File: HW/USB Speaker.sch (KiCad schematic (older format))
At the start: 1 part, among them U1 PCM2707C

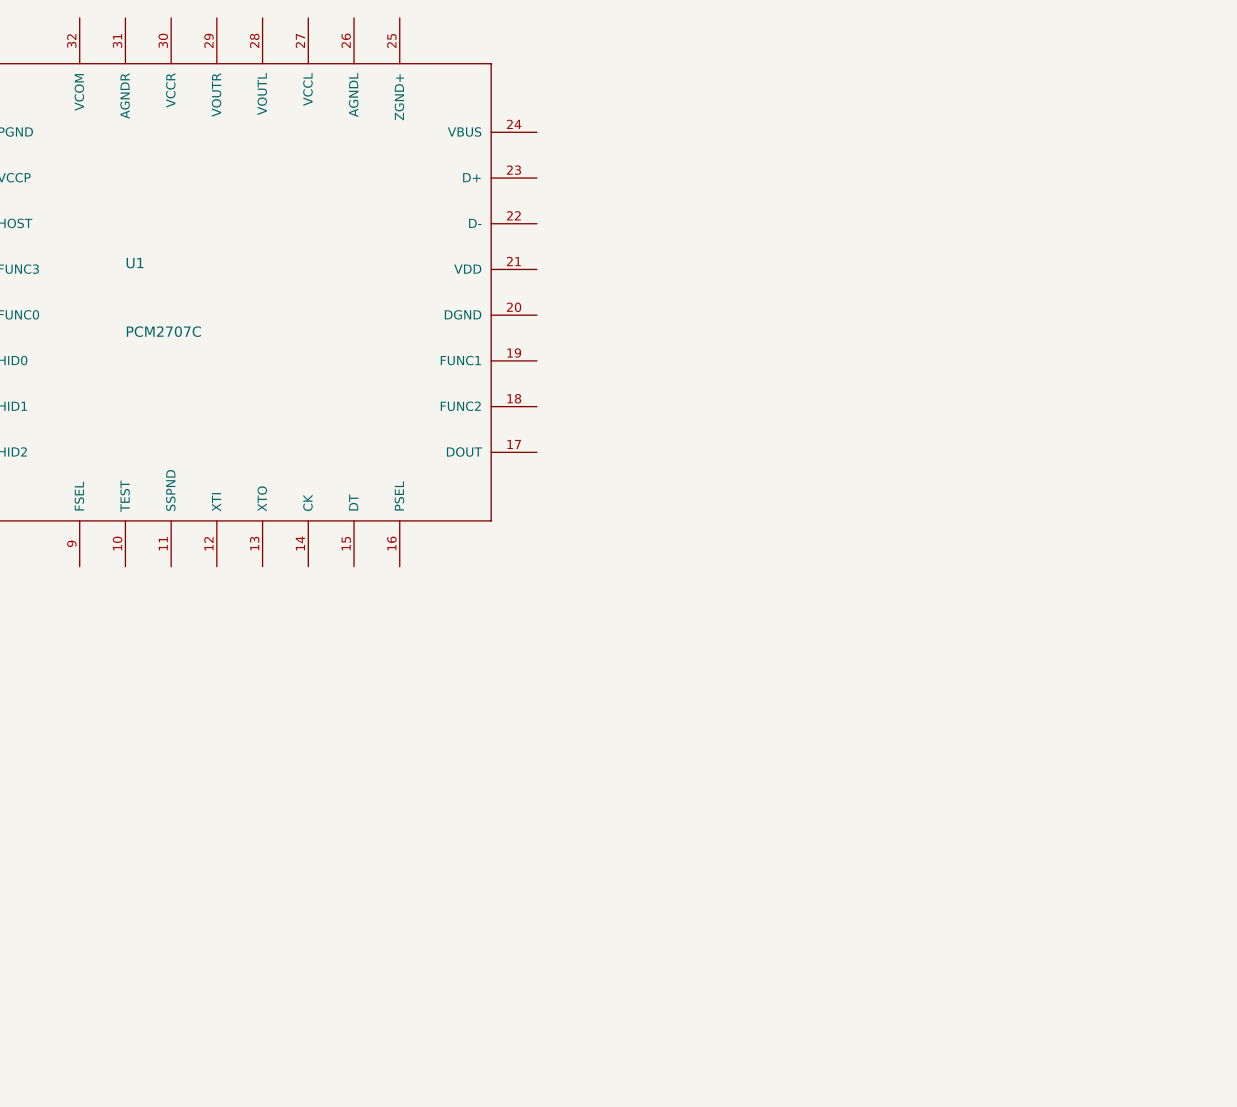
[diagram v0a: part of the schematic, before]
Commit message: Clock and USB circuits
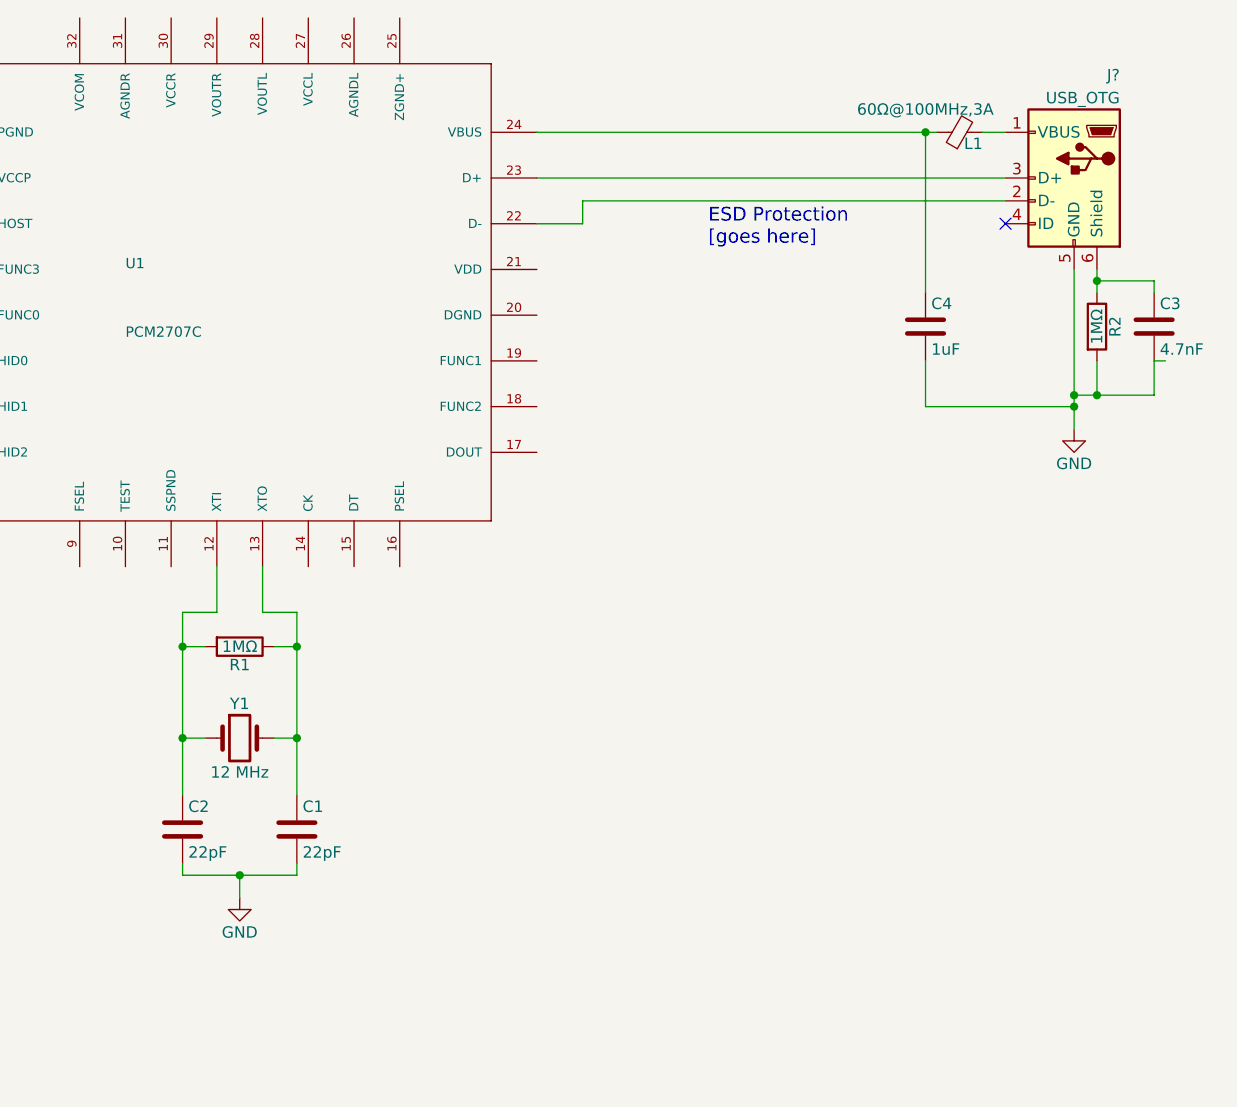
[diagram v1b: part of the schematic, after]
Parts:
- added C1, C2: 22pF, symbol C
- added C3: 4.7nF, symbol C
- added C4: 1uF, symbol C
- added J?: USB_OTG, symbol USB_OTG
- added L1: 60Ω@100MHz,3A, symbol Ferrite_Bead_Small
- added R1, R2: 1MΩ, symbol R
- added Y1: 12 MHz, symbol Crystal
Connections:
- net at U1.12 (XTI): now also C2.1, R1.2, Y1.1
- net at U1.13 (XTO): now also C1.1, R1.1, Y1.2
- net at U1.22 (D-): now also J?.2 (D-)
- net at U1.23 (D+): now also J?.3 (D+)
- net at U1.24 (VBUS): now also C4.1, L1.1
- new net: J?.1 (VBUS), L1.2
- new net: C3.1, J?.6 (Shield), R2.1
- new net GND: C1.2, C2.2, C3.2, C4.2, J?.5 (GND), R2.2
- no-connect marks 0 -> 1
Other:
- note added: "ESD Protection\n[goes here]\n"
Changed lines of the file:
@@
 LIBS:valves
 LIBS:PCM2707
+LIBS:USB Speaker-cache
 EELAYER 25 0
 EELAYER END
@@
 	1    0    0    -1
 $EndComp
+$Comp
+L Crystal Y1
+U 1 1 5B18799E
+P 5600 5250
+F 0 "Y1" H 5600 5400 50  0000 C CNN
+F 1 "12 MHz" H 5600 5100 50  0000 C CNN
+F 2 "" H 5600 5250 50  0001 C CNN
+F 3 "" H 5600 5250 50  0001 C CNN
+	1    5600 5250
+	1    0    0    -1
+$EndComp
+Wire Wire Line
+	5700 4500 5700 4700
+Wire Wire Line
+	5700 4700 5850 4700
+Wire Wire Line
+	5500 4700 5500 4500
+Wire Wire Line
+	5350 4700 5500 4700
+Wire Wire Line
+	5350 4700 5350 5500
+$Comp
+L R R1
+U 1 1 5B187A93
+P 5600 4850
+F 0 "R1" V 5680 4850 50  0000 C CNN
+F 1 "1MΩ" V 5600 4850 50  0000 C CNN
+F 2 "" V 5530 4850 50  0001 C CNN
+F 3 "" H 5600 4850 50  0001 C CNN
+	1    5600 4850
+	0    1    1    0
+$EndComp
+Wire Wire Line
+	5850 5250 5750 5250
+Wire Wire Line
+	5350 5250 5450 5250
+Wire Wire Line
+	5450 4850 5350 4850
+Connection ~ 5350 4850
+Wire Wire Line
+	5750 4850 5850 4850
+Connection ~ 5850 4850
+$Comp
+L C C2
+U 1 1 5B187E21
+P 5350 5650
+F 0 "C2" H 5375 5750 50  0000 L CNN
+F 1 "22pF" H 5375 5550 50  0000 L CNN
+F 2 "" H 5388 5500 50  0001 C CNN
+F 3 "" H 5350 5650 50  0001 C CNN
+	1    5350 5650
+	1    0    0    -1
+$EndComp
+$Comp
+L C C1
+U 1 1 5B187E62
+P 5850 5650
+F 0 "C1" H 5875 5750 50  0000 L CNN
+F 1 "22pF" H 5875 5550 50  0000 L CNN
+F 2 "" H 5888 5500 50  0001 C CNN
+F 3 "" H 5850 5650 50  0001 C CNN
+	1    5850 5650
+	1    0    0    -1
+$EndComp
+Connection ~ 5850 5250
+Connection ~ 5350 5250
+$Comp
+L GND #PWR?
+U 1 1 5B187EF0
+P 5600 5950
+F 0 "#PWR?" H 5600 5700 50  0001 C CNN
+F 1 "GND" H 5600 5800 50  0000 C CNN
+F 2 "" H 5600 5950 50  0001 C CNN
+F 3 "" H 5600 5950 50  0001 C CNN
+	1    5600 5950
+	1    0    0    -1
+$EndComp
+Wire Wire Line
+	5600 5950 5600 5850
+Wire Wire Line
+	5350 5850 5850 5850
+Wire Wire Line
+	5350 5850 5350 5800
+Wire Wire Line
+	5850 5850 5850 5800
+Connection ~ 5600 5850
+Wire Wire Line
+	5850 4700 5850 5500
+$Comp
+L USB_OTG J?
+U 1 1 5B18860C
+P 9250 2800
+F 0 "J?" H 9050 3250 50  0000 L CNN
+F 1 "USB_OTG" H 9050 3150 50  0000 L CNN
+F 2 "" H 9400 2750 50  0001 C CNN
+F 3 "" H 9400 2750 50  0001 C CNN
+	1    9250 2800
+	-1   0    0    -1
+$EndComp
+$Comp
+L GND #PWR?
+U 1 1 5B188764
+P 9250 3900
+F 0 "#PWR?" H 9250 3650 50  0001 C CNN
+F 1 "GND" H 9250 3750 50  0000 C CNN
+F 2 "" H 9250 3900 50  0001 C CNN
+F 3 "" H 9250 3900 50  0001 C CNN
+	1    9250 3900
+	1    0    0    -1
+$EndComp
+$Comp
+L R R2
+U 1 1 5B1887B9
+P 9350 3450
+F 0 "R2" V 9430 3450 50  0000 C CNN
+F 1 "1MΩ" V 9350 3450 50  0000 C CNN
+F 2 "" V 9280 3450 50  0001 C CNN
+F 3 "" H 9350 3450 50  0001 C CNN
+	1    9350 3450
+	1    0    0    -1
+$EndComp
+Wire Wire Line
+	9250 3200 9250 3900
+Wire Wire Line
+	9250 3750 9600 3750
+Wire Wire Line
+	9350 3200 9350 3300
+Wire Wire Line
+	9350 3750 9350 3600
+Connection ~ 9250 3800
+$Comp
+L C C3
+U 1 1 5B188B22
+P 9600 3450
+F 0 "C3" H 9625 3550 50  0000 L CNN
+F 1 "4.7nF" H 9625 3350 50  0000 L CNN
+F 2 "" H 9638 3300 50  0001 C CNN
+F 3 "" H 9600 3450 50  0001 C CNN
+	1    9600 3450
+	1    0    0    -1
+$EndComp
+Wire Wire Line
+	9600 3250 9600 3300
+Wire Wire Line
+	9600 3250 9350 3250
+Connection ~ 9350 3250
+Wire Wire Line
+	9600 3600 9650 3600
+Wire Wire Line
+	9600 3750 9600 3600
+Connection ~ 9350 3750
+NoConn ~ 8950 3000
+$Comp
+L C C4
+U 1 1 5B189480
+P 8600 3450
+F 0 "C4" H 8625 3550 50  0000 L CNN
+F 1 "1uF" H 8625 3350 50  0000 L CNN
+F 2 "" H 8638 3300 50  0001 C CNN
+F 3 "" H 8600 3450 50  0001 C CNN
+	1    8600 3450
+	1    0    0    -1
+$EndComp
+Wire Wire Line
+	8600 3600 8600 3800
+$Comp
+L Ferrite_Bead_Small L1
+U 1 1 5B1895A4
+P 8750 2600
+F 0 "L1" V 8700 2500 50  0000 L CNN
+F 1 "60Ω@100MHz,3A" V 8850 3050 50  0000 R CNN
+F 2 "" V 8680 2600 50  0001 C CNN
+F 3 "" H 8750 2600 50  0001 C CNN
+	1    8750 2600
+	0    -1   -1   0
+$EndComp
+Wire Wire Line
+	8950 2600 8850 2600
+Wire Wire Line
+	6900 2800 8950 2800
+Wire Wire Line
+	8950 2900 7100 2900
+Wire Wire Line
+	7100 2900 7100 3000
+Wire Wire Line
+	7100 3000 6900 3000
+Text Notes 7650 3100 0    60   ~ 0
+ESD Protection\n[goes here]\n
+Wire Wire Line
+	6900 2600 8650 2600
+Wire Wire Line
+	8600 3300 8600 2600
+Connection ~ 8600 2600
+Connection ~ 9250 3750
+Wire Wire Line
+	8600 3800 9250 3800
 $EndSCHEMATC

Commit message: DAC circuit
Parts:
- added C10, C11: 0.022uF, symbol C
- added C12, C13: 100uF, symbol CP1
- added C5, C6, C7, C9: 1uF, symbol C
- added C8: 10uF, symbol CP1
- added L2, L3: 60Ω@100MHz,3A, symbol Ferrite_Bead_Small
- added R10, R11, R12, R9: 3.3K, symbol R
- added R3, R6: 1.5K, symbol R
- added R4, R5: 22, symbol R
- added R7, R8: 16, symbol R
- R2: value 1MΩ -> 1M
- gave numbers to parts that had none: 1
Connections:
- net GND: now also U1.20 (DGND), U1.25 (ZGND+), C9.2, L2.2, L3.2, R10.2, R11.2, R12.2, R7.2, R8.2, R9.2
- net AGND_DAC: now reaches U1.1 (PGND)
- net AGND_DAC: now also C7.2, C8.2, L3.1
- net VDD: now reaches U1.10 (TEST)
- net VDD: now also U1.16 (PSEL), U1.21 (VDD), U1.3 (HOST), C9.1, R3.1, R6.1
- net at U1.15 (DT): now also R3.2
- net at U1.2 (VCCP): now also C7.1
- net at U1.22 (D-): now also R5.2; no longer J1.2 (D-)
- net at U1.23 (D+): now also R4.2; no longer J1.3 (D+)
- net AGND_LR: now reaches U1.26 (AGNDL)
- net AGND_LR: now also U1.31 (AGNDR), C5.1, C6.1, L2.1
- net at U1.27 (VCCL): now also C5.2
- net at U1.28 (VOUTL): now also C11.1, C13.1, R10.1
- net at U1.29 (VOUTR): now also C10.1, C12.1, R9.1
- net at U1.30 (VCCR): now also C6.2
- net at U1.32 (VCOM): now also C8.1
- new net: C10.2, R7.1
- new net: C11.2, R8.1
- new net: C12.2, R11.1
- new net: C13.2, R12.1
- new net USB_Dn: J1.2 (D-), R5.1
- new net USB_Dp: J1.3 (D+), R4.1, R6.2
- no-connect marks 1 -> 2
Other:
- moved on the sheet: C1, C2, C3, C4, J1, L1, R1, R2, U1, Y1

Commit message: DAC circuit edits and op-amp symbol creation
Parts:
- added R13: NP, symbol R
- added R14: 0.0, symbol R
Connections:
- net GND: now also R14.2
- net VDD: now also R13.1; no longer U1.3 (HOST)
- net SSPNDn: now reaches U1.11 (SSPND)
- net DOUT: now reaches U1.17 (DOUT)
- net FUNC2: now reaches U1.18 (FUNC2)
- net FUNC1: now reaches U1.19 (FUNC1)
- net FUNC3: now reaches U1.4 (FUNC3)
- net FUNC0: now reaches U1.5 (FUNC0)
- net HID0: now reaches U1.6 (HID0)
- net HID1: now reaches U1.7 (HID1)
- net HID2: now reaches U1.8 (HID2)
- net FSEL: now reaches U1.9 (FSEL)
- net Vout_L: now reaches C12.2, R11.1
- net Vout_R: now reaches C13.2, R12.1
- new net: R13.2, R14.1, U1.3 (HOST)
- no-connect marks 2 -> 11
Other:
- moved on the sheet: C7, L3

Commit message: Amplifier circuit using TPA6211A1-Q1
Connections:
- net VBUS: now reaches C4.1, L1.1, U1.24 (VBUS)
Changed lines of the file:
@@
 L VDD #PWR?
 U 1 1 5B1A7528
-P 5900 2400
-F 0 "#PWR?" H 5900 2250 50  0001 C CNN
-F 1 "VDD" H 5900 2550 50  0000 C CNN
-F 2 "" H 5900 2400 50  0001 C CNN
-F 3 "" H 5900 2400 50  0001 C CNN
-	1    5900 2400
+P 5900 2500
+F 0 "#PWR?" H 5900 2350 50  0001 C CNN
+F 1 "VDD" H 5900 2650 50  0000 C CNN
+F 2 "" H 5900 2500 50  0001 C CNN
+F 3 "" H 5900 2500 50  0001 C CNN
+	1    5900 2500
 	1    0    0    -1
 $EndComp
@@
 	3850 5100 4000 5100
 Wire Wire Line
-	3850 5100 3850 5900
+	3850 5100 3850 5250
+Wire Wire Line
+	3850 5250 3850 5650
+Wire Wire Line
+	3850 5650 3850 5900
 Wire Wire Line
 	4350 5650 4250 5650
@@
 	4100 6350 4100 6250
 Wire Wire Line
-	3850 6250 4350 6250
+	3850 6250 4100 6250
+Wire Wire Line
+	4100 6250 4350 6250
 Wire Wire Line
 	3850 6250 3850 6200
@@
 Connection ~ 4100 6250
 Wire Wire Line
-	4350 5100 4350 5900
-Wire Wire Line
-	7750 3600 7750 4300
-Wire Wire Line
-	7750 4150 8100 4150
-Wire Wire Line
-	7850 3600 7850 3700
+	4350 5100 4350 5250
+Wire Wire Line
+	4350 5250 4350 5650
+Wire Wire Line
+	4350 5650 4350 5900
+Wire Wire Line
+	7750 3600 7750 4150
+Wire Wire Line
+	7750 4150 7750 4200
+Wire Wire Line
+	7750 4200 7750 4300
+Wire Wire Line
+	7750 4150 7850 4150
+Wire Wire Line
+	7850 4150 8100 4150
+Wire Wire Line
+	7850 3600 7850 3650
+Wire Wire Line
+	7850 3650 7850 3700
 Wire Wire Line
 	7850 4150 7850 4000
@@
 	7450 3000 7350 3000
 Wire Wire Line
-	5400 3000 7150 3000
+	5400 3000 5650 3000
+Wire Wire Line
+	5650 3000 7100 3000
+Wire Wire Line
+	7100 3000 7150 3000
 Wire Wire Line
 	7100 3700 7100 3000
@@
 	7100 4200 7750 4200
 Wire Wire Line
-	3600 1800 5050 1800
+	3600 1800 3800 1800
+Wire Wire Line
+	3800 1800 4400 1800
+Wire Wire Line
+	4400 1800 4600 1800
+Wire Wire Line
+	4600 1800 5050 1800
 Wire Wire Line
 	3600 1800 3600 2500
@@
 Connection ~ 3800 1800
 Wire Wire Line
-	1650 2750 1650 3350
+	1650 2750 1650 3000
+Wire Wire Line
+	1650 3000 1650 3200
+Wire Wire Line
+	1650 3200 1650 3350
 Wire Wire Line
 	1900 3200 1650 3200
@@
 	4800 5100 5400 5100
 Wire Wire Line
-	5400 4900 5400 5200
+	5400 4900 5400 5100
+Wire Wire Line
+	5400 5100 5400 5200
 Wire Wire Line
 	2200 3200 2800 3200
@@
 	6450 3650 6450 3600
 Wire Wire Line
-	6050 3650 6450 3650
+	6050 3650 6300 3650
+Wire Wire Line
+	6300 3650 6450 3650
 Wire Wire Line
 	6300 3650 6300 3700
@@
 	6050 3800 6050 4050
 Wire Wire Line
-	6300 4000 6300 4100
+	6300 4000 6300 4050
+Wire Wire Line
+	6300 4050 6300 4100
 Wire Wire Line
 	6050 4050 6300 4050
@@
 	5400 3400 5500 3400
 Wire Wire Line
-	5800 3200 7450 3200
+	5800 3200 5900 3200
+Wire Wire Line
+	5900 3200 7450 3200
 Wire Wire Line
 	5800 3400 5900 3400
@@
 	2750 3000 2750 3000
 Wire Wire Line
-	5900 2400 5900 2550
+	5900 2500 5900 2550
 Wire Wire Line
 	5900 2850 5900 3200
@@
 	4000 850  4000 2500
 Wire Wire Line
-	4000 850  7550 850
+	4000 850  6200 850
+Wire Wire Line
+	6200 850  7150 850
+Wire Wire Line
+	7150 850  7550 850
 Wire Wire Line
 	4200 1100 4200 2500
 Wire Wire Line
-	4200 1100 7550 1100
-Wire Wire Line
-	7850 850  8900 850
-Wire Wire Line
-	7850 1100 8900 1100
+	4200 1100 6650 1100
+Wire Wire Line
+	6650 1100 7350 1100
+Wire Wire Line
+	7350 1100 7550 1100
+Wire Wire Line
+	7850 850  8200 850
+Wire Wire Line
+	8200 850  8900 850
+Wire Wire Line
+	7850 1100 8400 1100
+Wire Wire Line
+	8400 1100 8900 1100
 Wire Wire Line
 	6200 1200 6200 850
@@
 	2050 3950 750  3950
 Wire Wire Line
-	750  3800 750  4050
+	750  3800 750  3950
+Wire Wire Line
+	750  3950 750  4050
 $Comp
 L R R13
@@
 NoConn ~ 2350 4400
 NoConn ~ 2850 5000
+$Comp
+L VBUS #PWR?
+U 1 1 5B2872F3
+P 5650 2500
+F 0 "#PWR?" H 5650 2350 50  0001 C CNN
+F 1 "VBUS" H 5650 2650 50  0000 C CNN
+F 2 "" H 5650 2500 50  0001 C CNN
+F 3 "" H 5650 2500 50  0001 C CNN
+	1    5650 2500
+	1    0    0    -1
+$EndComp
+Wire Wire Line
+	5650 2500 5650 3000
+Connection ~ 5650 3000
 $EndSCHEMATC

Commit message: Switching out 2x TPA6211A1 for 1x TPA3137D2
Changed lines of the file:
@@
 	3850 5100 4000 5100
 Wire Wire Line
-	3850 5100 3850 5250
-Wire Wire Line
-	3850 5250 3850 5650
-Wire Wire Line
-	3850 5650 3850 5900
+	3850 5100 3850 5900
 Wire Wire Line
 	4350 5650 4250 5650
@@
 	4100 6350 4100 6250
 Wire Wire Line
-	3850 6250 4100 6250
-Wire Wire Line
-	4100 6250 4350 6250
+	3850 6250 4350 6250
 Wire Wire Line
 	3850 6250 3850 6200
@@
 Connection ~ 4100 6250
 Wire Wire Line
-	4350 5100 4350 5250
-Wire Wire Line
-	4350 5250 4350 5650
-Wire Wire Line
-	4350 5650 4350 5900
-Wire Wire Line
-	7750 3600 7750 4150
-Wire Wire Line
-	7750 4150 7750 4200
-Wire Wire Line
-	7750 4200 7750 4300
-Wire Wire Line
-	7750 4150 7850 4150
-Wire Wire Line
-	7850 4150 8100 4150
-Wire Wire Line
-	7850 3600 7850 3650
-Wire Wire Line
-	7850 3650 7850 3700
+	4350 5100 4350 5900
+Wire Wire Line
+	7750 3600 7750 4300
+Wire Wire Line
+	7750 4150 8100 4150
+Wire Wire Line
+	7850 3600 7850 3700
 Wire Wire Line
 	7850 4150 7850 4000
@@
 	7450 3000 7350 3000
 Wire Wire Line
-	5400 3000 5650 3000
-Wire Wire Line
-	5650 3000 7100 3000
-Wire Wire Line
-	7100 3000 7150 3000
+	5400 3000 7150 3000
 Wire Wire Line
 	7100 3700 7100 3000
@@
 	7100 4200 7750 4200
 Wire Wire Line
-	3600 1800 3800 1800
-Wire Wire Line
-	3800 1800 4400 1800
-Wire Wire Line
-	4400 1800 4600 1800
-Wire Wire Line
-	4600 1800 5050 1800
+	3600 1800 5050 1800
 Wire Wire Line
 	3600 1800 3600 2500
@@
 Connection ~ 3800 1800
 Wire Wire Line
-	1650 2750 1650 3000
-Wire Wire Line
-	1650 3000 1650 3200
-Wire Wire Line
-	1650 3200 1650 3350
+	1650 2750 1650 3350
 Wire Wire Line
 	1900 3200 1650 3200
@@
 	4800 5100 5400 5100
 Wire Wire Line
-	5400 4900 5400 5100
-Wire Wire Line
-	5400 5100 5400 5200
+	5400 4900 5400 5200
 Wire Wire Line
 	2200 3200 2800 3200
@@
 	6450 3650 6450 3600
 Wire Wire Line
-	6050 3650 6300 3650
-Wire Wire Line
-	6300 3650 6450 3650
+	6050 3650 6450 3650
 Wire Wire Line
 	6300 3650 6300 3700
@@
 	6050 3800 6050 4050
 Wire Wire Line
-	6300 4000 6300 4050
-Wire Wire Line
-	6300 4050 6300 4100
+	6300 4000 6300 4100
 Wire Wire Line
 	6050 4050 6300 4050
@@
 	5400 3400 5500 3400
 Wire Wire Line
-	5800 3200 5900 3200
-Wire Wire Line
-	5900 3200 7450 3200
+	5800 3200 7450 3200
 Wire Wire Line
 	5800 3400 5900 3400
@@
 	4000 850  4000 2500
 Wire Wire Line
-	4000 850  6200 850
-Wire Wire Line
-	6200 850  7150 850
-Wire Wire Line
-	7150 850  7550 850
+	4000 850  7550 850
 Wire Wire Line
 	4200 1100 4200 2500
 Wire Wire Line
-	4200 1100 6650 1100
-Wire Wire Line
-	6650 1100 7350 1100
-Wire Wire Line
-	7350 1100 7550 1100
-Wire Wire Line
-	7850 850  8200 850
-Wire Wire Line
-	8200 850  8900 850
-Wire Wire Line
-	7850 1100 8400 1100
-Wire Wire Line
-	8400 1100 8900 1100
+	4200 1100 7550 1100
+Wire Wire Line
+	7850 850  8900 850
+Wire Wire Line
+	7850 1100 8900 1100
 Wire Wire Line
 	6200 1200 6200 850
@@
 	2050 3950 750  3950
 Wire Wire Line
-	750  3800 750  3950
-Wire Wire Line
-	750  3950 750  4050
+	750  3800 750  4050
 $Comp
 L R R13

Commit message: Finsihed drawing amp circuit. Adding options and values later
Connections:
- net Vout_L renamed Speaker Op-Amp Circuit/Vin_R
- net Vout_R renamed Speaker Op-Amp Circuit/Vin_L
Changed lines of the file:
@@
 Connection ~ 7850 3650
-Wire Wire Line
-	8100 4000 8150 4000
 Wire Wire Line
 	8100 4150 8100 4000
@@
 	4200 1100 7550 1100
 Wire Wire Line
-	7850 850  8900 850
-Wire Wire Line
-	7850 1100 8900 1100
+	7850 850  9400 850
+Wire Wire Line
+	7850 1100 9400 1100
 Wire Wire Line
 	6200 1200 6200 850
@@
 Wire Wire Line
 	3800 5450 2850 5450
-Text GLabel 8900 850  2    60   Input ~ 0
-Vout_L
-Text GLabel 8900 1100 2    60   Input ~ 0
-Vout_R
 Wire Wire Line
 	2800 3400 2050 3400
@@
 Wire Wire Line
 	750  4450 750  4350
-Text GLabel 2850 5450 0    60   Input ~ 0
-SSPNDn
 $Sheet
 S 9400 600  1750 1150
@@
 F0 "Speaker Op-Amp Circuit" 60
 F1 "USB_Speaker_page2.sch" 60
+F2 "Vin_R" I L 9400 850 60
+F3 "Vin_L" I L 9400 1100 60
 $EndSheet
 NoConn ~ 5850 4000
@@
 	5650 2500 5650 3000
 Connection ~ 5650 3000
+Text Label 2850 5450 0    60   ~ 0
+SSPNDn
 $EndSCHEMATC

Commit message: ferrite chosen
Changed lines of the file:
@@
 F2 "Vin_R" I L 9400 850 60
 F3 "Vin_L" I L 9400 1100 60
+F4 "SSPNDn" I L 9400 1350 60
 $EndSheet
 NoConn ~ 5850 4000
@@
 Text Label 2850 5450 0    60   ~ 0
 SSPNDn
+Wire Wire Line
+	9400 1350 8750 1350
+Text Label 8750 1350 0    60   ~ 0
+SSPNDn
 $EndSCHEMATC
